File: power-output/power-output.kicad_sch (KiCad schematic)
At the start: 26 parts, among them P1 USB_C_Plug_USB2.0, U1 AP2112K-3.3, U2 FUSB302BMPX, U3 LM78L05_SO8, U4 ESP8266EX, U5 CP2102N-Axx-xQFN28

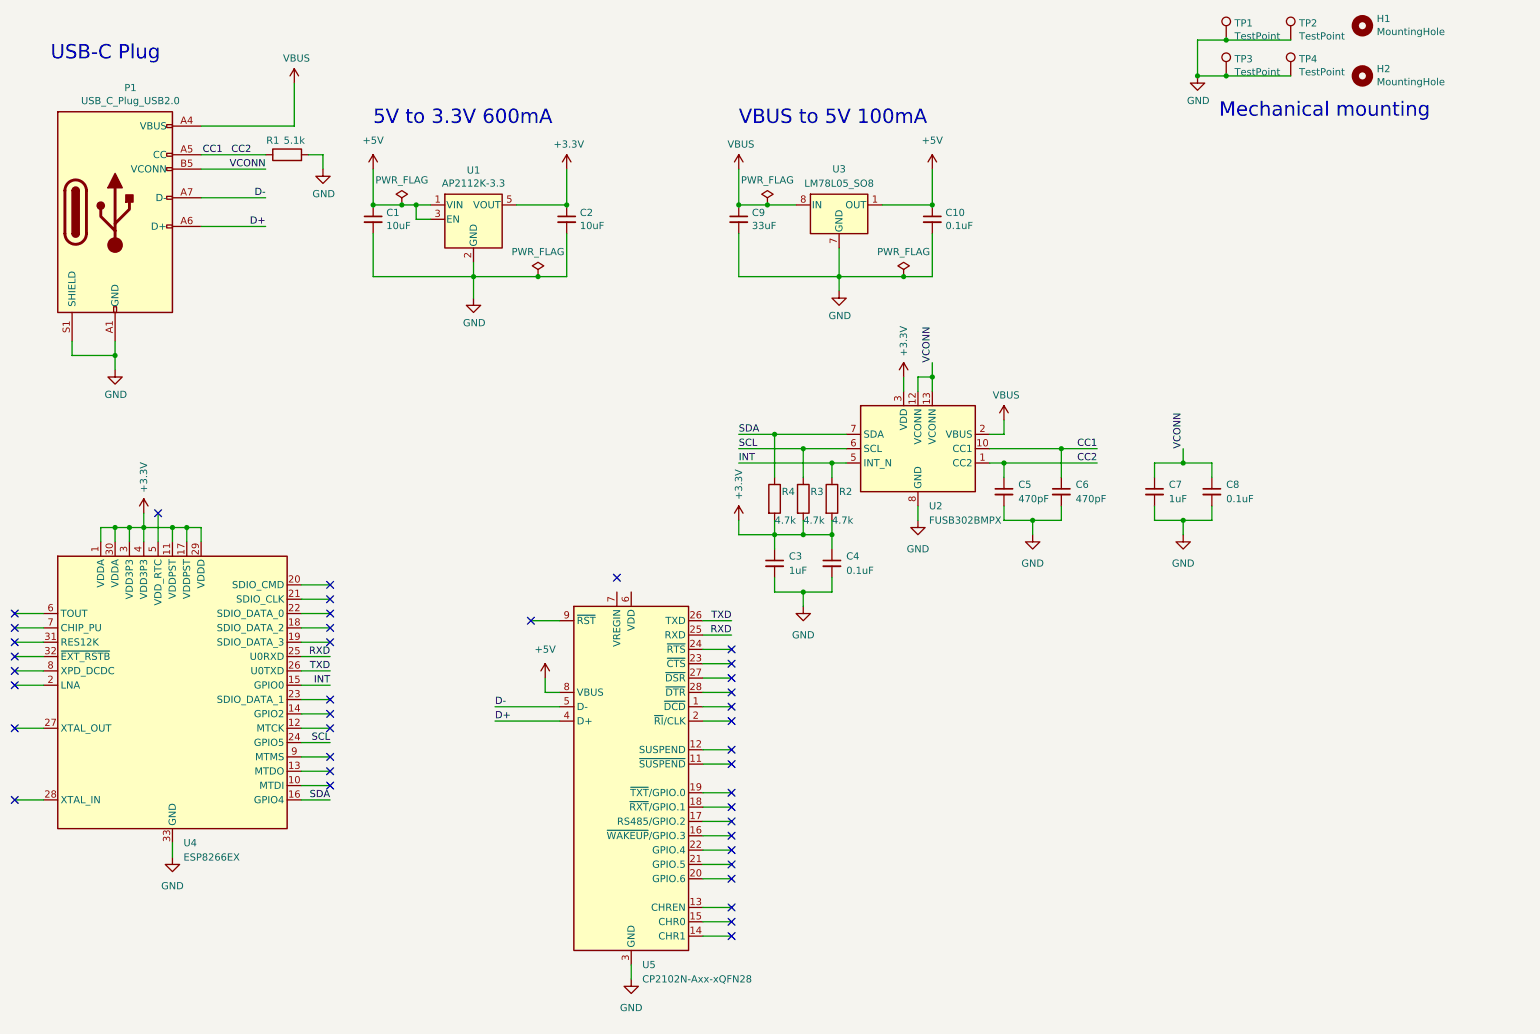
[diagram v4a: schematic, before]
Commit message: Labeled everything in schmatic
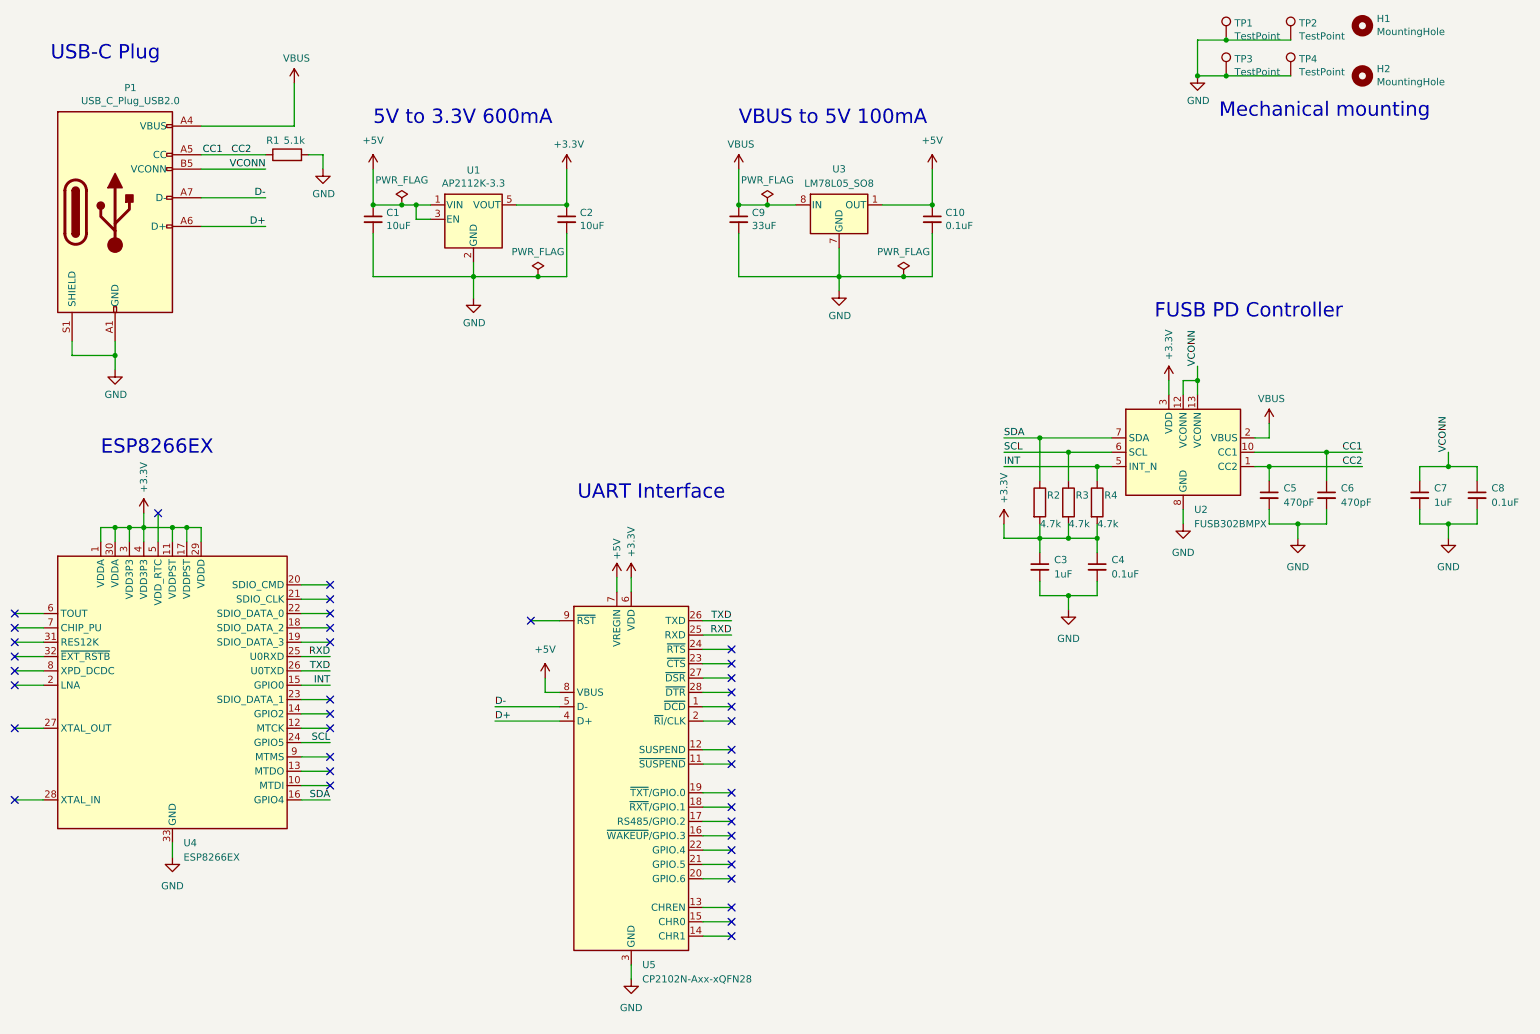
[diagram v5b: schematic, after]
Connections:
- net +3.3V: now also U5.6 (VDD)
- net +5V: now also U5.7 (VREGIN)
- net INT: now also R4.1; no longer R2.1
- net SDA: now also R2.1; no longer R4.1
- no-connect marks 40 -> 39
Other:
- note added: "ESP8266EX"
- note added: "FUSB PD Controller"
- note added: "UART Interface"

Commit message: Updated Schematic
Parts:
- added J1: Conn_01x02_Socket, symbol Connector:Conn_01x02_Socket
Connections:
- net GND: now also J1.2 (Pin_2)
- net VBUS: now also J1.1 (Pin_1)
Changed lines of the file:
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@@
+    (stroke (width 0) (type default))
+  )
+  (wire (pts (xy 226.695 139.7) (xy 224.155 139.7))
     (stroke (width 0) (type default))
   )
@@
     (stroke (width 0) (type default))
   )
+  (wire (pts (xy 224.155 139.7) (xy 224.155 137.16))
+    (stroke (width 0) (type default))
+  )
   (wire (pts (xy 210.82 111.125) (xy 215.9 111.125))
     (stroke (width 0) (type default))
@@
     (stroke (width 0) (type default))
   )
+  (wire (pts (xy 224.155 142.24) (xy 224.155 144.78))
+    (stroke (width 0) (type default))
+  )
   (wire (pts (xy 87.63 64.77) (xy 105.41 64.77))
     (stroke (width 0) (type default))
@@
   )
   (wire (pts (xy 205.74 111.125) (xy 205.74 113.665))
+    (stroke (width 0) (type default))
+  )
+  (wire (pts (xy 226.695 142.24) (xy 224.155 142.24))
     (stroke (width 0) (type default))
   )
@@
     )
   )
+  (symbol (lib_id "Connector:Conn_01x02_Socket") (at 231.775 139.7 0) (unit 1)
+    (in_bom yes) (on_board yes) (dnp no) (fields_autoplaced)
+    (property "Reference" "J1" (at 233.68 139.7 0)
+      (effects (font (size 1.27 1.27)) (justify left))
+    )
+    (property "Value" "Conn_01x02_Socket" (at 233.68 142.24 0)
+      (effects (font (size 1.27 1.27)) (justify left))
+    )
+    (property "Footprint" "" (at 231.775 139.7 0)
+      (effects (font (size 1.27 1.27)) hide)
+    )
+    (property "Datasheet" "~" (at 231.775 139.7 0)
+      (effects (font (size 1.27 1.27)) hide)
+    )
+    (pin "1")
+    (pin "2")
+    (instances
+      (project "power-output"
+        (path "/4f0a983c-a4cb-4169-a6c2-393f2a3719c6"
+          (reference "J1") (unit 1)
+        )
+      )
+    )
+  )
   (symbol (lib_id "power:+5V") (at 130.81 118.11 0) (unit 1)
     (in_bom yes) (on_board yes) (dnp no)
@@
         (path "/4f0a983c-a4cb-4169-a6c2-393f2a3719c6"
           (reference "#PWR021") (unit 1)
+        )
+      )
+    )
+  )
+  (symbol (lib_id "power:VBUS") (at 224.155 137.16 0) (unit 1)
+    (in_bom yes) (on_board yes) (dnp no) (fields_autoplaced)
+    (property "Reference" "#PWR024" (at 224.155 140.97 0)
+      (effects (font (size 1.27 1.27)) hide)
+    )
+    (property "Value" "VBUS" (at 224.155 132.08 0)
+      (effects (font (size 1.27 1.27)))
+    )
+    (property "Footprint" "" (at 224.155 137.16 0)
+      (effects (font (size 1.27 1.27)) hide)
+    )
+    (property "Datasheet" "" (at 224.155 137.16 0)
+      (effects (font (size 1.27 1.27)) hide)
+    )
+    (pin "1")
+    (instances
+      (project "power-output"
+        (path "/4f0a983c-a4cb-4169-a6c2-393f2a3719c6"
+          (reference "#PWR024") (unit 1)
         )
       )
@@
         )
       )
+    )
+  )
+  (symbol (lib_id "power:GND") (at 224.155 144.78 0) (unit 1)
+    (in_bom yes) (on_board yes) (dnp no) (fields_autoplaced)
+    (property "Reference" "#PWR023" (at 224.155 151.13 0)
+      (effects (font (size 1.27 1.27)) hide)
+    )
+    (property "Value" "GND" (at 224.155 149.86 0)
+      (effects (font (size 1.27 1.27)))
+    )
+    (property "Footprint" "" (at 224.155 144.78 0)
+      (effects (font (size 1.27 1.27)) hide)
+    )
+    (property "Datasheet" "" (at 224.155 144.78 0)
+      (effects (font (size 1.27 1.27)) hide)
+    )
+    (pin "1")
+    (instances
+      (project "power-output"
+        (path "/4f0a983c-a4cb-4169-a6c2-393f2a3719c6"
+          (reference "#PWR023") (unit 1)
+        )
+      )
